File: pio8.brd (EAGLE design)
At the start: 37 x 37 mm, 35 parts, among them IC1 DS2408, X1 MSTBV3, X7 MSTBV5, X8 MSTBV5

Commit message: changing some values: 5 Ohm resistor to 5.1 Ohm (5 Ohm is not broadly available) selected different type of TVS diode with essentially the same ratings
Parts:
- D1, D10, D11, D2, D3, D4, D5, D6, D7, D8: value SMA6F7.5A -> SMAJ7.5A-LF
- R1, R10, R11, R12, R13, R14, R15, R16, R19, R2: value 5 -> 5.1
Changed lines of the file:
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@@
 <attribute name="NAME" x="20.217" y="16.5" size="0.6096" layer="25" rot="R180"/>
 </element>
-<element name="R1" library="rcl" package="R0402" value="5" x="34.25" y="3.25" smashed="yes" rot="R90">
+<element name="R1" library="rcl" package="R0402" value="5.1" x="34.25" y="3.25" smashed="yes" rot="R90">
 <attribute name="NAME" x="35.025" y="3.847" size="0.6096" layer="25" rot="R270"/>
 </element>
-<element name="R2" library="rcl" package="R0402" value="5" x="27.5" y="6.75" smashed="yes" rot="R90">
+<element name="R2" library="rcl" package="R0402" value="5.1" x="27.5" y="6.75" smashed="yes" rot="R90">
 <attribute name="NAME" x="27.725" y="4.665" size="0.6096" layer="25" rot="R90"/>
 </element>
@@
 <attribute name="NAME" x="26.751" y="29.969" size="0.6096" layer="25"/>
 </element>
-<element name="D8" library="diodes" package="DO214AC" value="SMA6F7.5A" x="30" y="3" smashed="yes" rot="R180">
+<element name="D8" library="diodes" package="DO214AC" value="SMAJ7.5A-LF" x="30" y="3" smashed="yes" rot="R180">
 <attribute name="NAME" x="28.19" y="2.766" size="0.6096" layer="25" ratio="10"/>
 </element>
-<element name="D1" library="diodes" package="DO214AC" value="SMA6F7.5A" x="15" y="26" smashed="yes">
+<element name="D1" library="diodes" package="DO214AC" value="SMAJ7.5A-LF" x="15" y="26" smashed="yes">
 <attribute name="NAME" x="15.91" y="25.746" size="0.6096" layer="25" ratio="10"/>
 </element>
-<element name="D2" library="diodes" package="DO214AC" value="SMA6F7.5A" x="15" y="29" smashed="yes">
+<element name="D2" library="diodes" package="DO214AC" value="SMAJ7.5A-LF" x="15" y="29" smashed="yes">
 <attribute name="NAME" x="15.81" y="28.696" size="0.6096" layer="25" ratio="10"/>
 </element>
-<element name="D3" library="diodes" package="DO214AC" value="SMA6F7.5A" x="15" y="32" smashed="yes">
+<element name="D3" library="diodes" package="DO214AC" value="SMAJ7.5A-LF" x="15" y="32" smashed="yes">
 <attribute name="NAME" x="15.87" y="31.756" size="0.6096" layer="25" ratio="10"/>
 </element>
-<element name="D4" library="diodes" package="DO214AC" value="SMA6F7.5A" x="15" y="35" smashed="yes">
+<element name="D4" library="diodes" package="DO214AC" value="SMAJ7.5A-LF" x="15" y="35" smashed="yes">
 <attribute name="NAME" x="15.76" y="34.806" size="0.6096" layer="25" ratio="10"/>
 </element>
-<element name="D5" library="diodes" package="DO214AC" value="SMA6F7.5A" x="22" y="35" smashed="yes" rot="R180">
+<element name="D5" library="diodes" package="DO214AC" value="SMAJ7.5A-LF" x="22" y="35" smashed="yes" rot="R180">
 <attribute name="NAME" x="20.19" y="34.672" size="0.6096" layer="25" ratio="10"/>
 </element>
-<element name="D6" library="diodes" package="DO214AC" value="SMA6F7.5A" x="22" y="32" smashed="yes" rot="R180">
+<element name="D6" library="diodes" package="DO214AC" value="SMAJ7.5A-LF" x="22" y="32" smashed="yes" rot="R180">
 <attribute name="NAME" x="20.062" y="31.616" size="0.6096" layer="25" ratio="10"/>
 </element>
-<element name="D7" library="diodes" package="DO214AC" value="SMA6F7.5A" x="22" y="29" smashed="yes" rot="R180">
+<element name="D7" library="diodes" package="DO214AC" value="SMAJ7.5A-LF" x="22" y="29" smashed="yes" rot="R180">
 <attribute name="NAME" x="20.036" y="28.728" size="0.6096" layer="25" ratio="10"/>
 </element>
-<element name="R10" library="rcl" package="R0402" value="5" x="16.567" y="10.643" smashed="yes" rot="R270">
+<element name="R10" library="rcl" package="R0402" value="5.1" x="16.567" y="10.643" smashed="yes" rot="R270">
 <attribute name="NAME" x="15.808" y="9.882" size="0.6096" layer="25" rot="R90"/>
 </element>
-<element name="R11" library="rcl" package="R0402" value="5" x="17.837" y="21.816" smashed="yes" rot="R90">
+<element name="R11" library="rcl" package="R0402" value="5.1" x="17.837" y="21.816" smashed="yes" rot="R90">
 <attribute name="NAME" x="18.122" y="23.061" size="0.6096" layer="25" rot="R90"/>
 </element>
-<element name="R12" library="rcl" package="R0402" value="5" x="19.117" y="21.804" smashed="yes" rot="R90">
+<element name="R12" library="rcl" package="R0402" value="5.1" x="19.117" y="21.804" smashed="yes" rot="R90">
 <attribute name="NAME" x="19.462" y="23.139" size="0.6096" layer="25" rot="R90"/>
 </element>
-<element name="R13" library="rcl" package="R0402" value="5" x="20.377" y="21.816" smashed="yes" rot="R90">
+<element name="R13" library="rcl" package="R0402" value="5.1" x="20.377" y="21.816" smashed="yes" rot="R90">
 <attribute name="NAME" x="20.108" y="24.729" size="0.6096" layer="25" rot="R270"/>
 </element>
-<element name="R14" library="rcl" package="R0402" value="5" x="21.637" y="21.834" smashed="yes" rot="R90">
+<element name="R14" library="rcl" package="R0402" value="5.1" x="21.637" y="21.834" smashed="yes" rot="R90">
 <attribute name="NAME" x="21.792" y="23.239" size="0.6096" layer="25" rot="R90"/>
 </element>
-<element name="R15" library="rcl" package="R0402" value="5" x="24.157" y="21.774" smashed="yes" rot="R90">
+<element name="R15" library="rcl" package="R0402" value="5.1" x="24.157" y="21.774" smashed="yes" rot="R90">
 <attribute name="NAME" x="24.562" y="22.929" size="0.6096" layer="25" rot="R90"/>
 </element>
-<element name="R16" library="rcl" package="R0402" value="5" x="27.5" y="18.25" smashed="yes" rot="R90">
+<element name="R16" library="rcl" package="R0402" value="5.1" x="27.5" y="18.25" smashed="yes" rot="R90">
 <attribute name="NAME" x="27.865" y="15.615" size="0.6096" layer="25" rot="R90"/>
 </element>
@@
 <attribute name="NAME" x="26.615" y="27.012" size="0.6096" layer="25"/>
 </element>
-<element name="D10" library="diodes" package="DO214AC" value="SMA6F7.5A" x="22" y="26" smashed="yes" rot="R180">
+<element name="D10" library="diodes" package="DO214AC" value="SMAJ7.5A-LF" x="22" y="26" smashed="yes" rot="R180">
 <attribute name="NAME" x="20" y="25.5" size="0.6096" layer="25" ratio="10"/>
 </element>
-<element name="D11" library="diodes" package="DO214AC" value="SMA6F7.5A" x="27.01" y="11.96" smashed="yes" rot="R270">
+<element name="D11" library="diodes" package="DO214AC" value="SMAJ7.5A-LF" x="27.01" y="11.96" smashed="yes" rot="R270">
 <attribute name="NAME" x="27.454" y="9.9" size="0.6096" layer="25" ratio="10" rot="R90"/>
 </element>
-<element name="R19" library="rcl" package="R0402" value="5" x="26" y="18.25" smashed="yes" rot="R90">
+<element name="R19" library="rcl" package="R0402" value="5.1" x="26" y="18.25" smashed="yes" rot="R90">
 <attribute name="NAME" x="26.365" y="15.615" size="0.6096" layer="25" rot="R90"/>
 <attribute name="VALUE" x="27.905" y="17.615" size="1.27" layer="27" rot="R90"/>

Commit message: rotating connectors to resolve issue #1 while maintaining IO and GND/VCC pinout but rotating pinout for the one wire connector (to keep the pin numbering the same as other 1-wire devices have)
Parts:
- moved X1 0.70 mm to (18.5, 4.70), turned to 180 degrees
- moved X8 0.63 mm to (32.3, 18.5), turned to 270 degrees
- moved X7 0.60 mm to (4.70, 18.5), turned to 90 degrees
- moved D9 0.25 mm to (22.9, 10.4)
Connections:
- net GND: now also X8.5; no longer X8.1
- net N$1: now also X7.1; no longer X7.5
- net N$11: now also X8.4; no longer X8.2
- net N$2: now also X7.2; no longer X7.4
- net N$4: now also X7.4; no longer X7.2
- net N$5: now also X7.5; no longer X7.1
- net N$6: now also X8.1; no longer X8.5
- net N$7: now also X8.2; no longer X8.4
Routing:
- net N$9: track 8.07 -> 23.4 mm
- net N$10: track 18.8 -> 20.9 mm
- net N$20: track 24.3 -> 25.7 mm
- net GND: track 71.8 -> 70.5 mm
- net N$12: track 25.1 -> 25.8 mm
- net N$7: track 26.8 -> 26.2 mm
- net N$6: track 26.5 -> 25.9 mm
- net N$11: track 79.8 -> 79.2 mm
- net N$5: track 47.7 -> 47.1 mm
- net N$4: track 37.2 -> 36.6 mm
- net N$3: track 35.6 -> 35.0 mm
- net N$2: track 34.4 -> 33.8 mm
- net N$1: track 46.3 -> 45.7 mm

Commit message: changing the connector solution for the digital i/o's - now using spring clamp terminals instead of pluggable screw terminals. The new ones should reduce the width. Also turning back the 3 pin connector so that the screw terminal pints inward
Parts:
- removed X7, X8: MSTBV5, con-phoenix-508:MSTBV5
- added X2, X3: SPRING_CLAMP_5_AST215, connectors:AST215_5
- turned X1 to 0 degrees
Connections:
- net GND: now also X2.5A, X2.5B; no longer X8.5
- net N$1: now also X3.1A, X3.1B; no longer X7.1
- net N$11: now also X2.4A, X2.4B; no longer X8.4
- net N$12: now also X2.3A, X2.3B; no longer X8.3
- net N$2: now also X3.2A, X3.2B; no longer X7.2
- net N$3: now also X3.3A, X3.3B; no longer X7.3
- net N$4: now also X3.4A, X3.4B; no longer X7.4
- net N$5: now also X3.5A, X3.5B; no longer X7.5
- net N$6: now also X2.1A, X2.1B; no longer X8.1
- net N$7: now also X2.2A, X2.2B; no longer X8.2
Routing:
- net N$9: track 23.4 -> 8.36 mm
- net N$3: track 35.0 -> 44.7 mm
- net N$4: track 36.6 -> 46.1 mm
- net N$5: track 47.1 -> 56.0 mm
- net GND: track 70.5 -> 62.9 mm
- net N$7: track 26.2 -> 30.3 mm
- net N$12: track 25.8 -> 29.8 mm
- net N$6: track 25.9 -> 28.9 mm
- net N$2: track 33.8 -> 36.8 mm
- net N$11: track 79.2 -> 82.1 mm
- net N$1: track 45.7 -> 48.6 mm

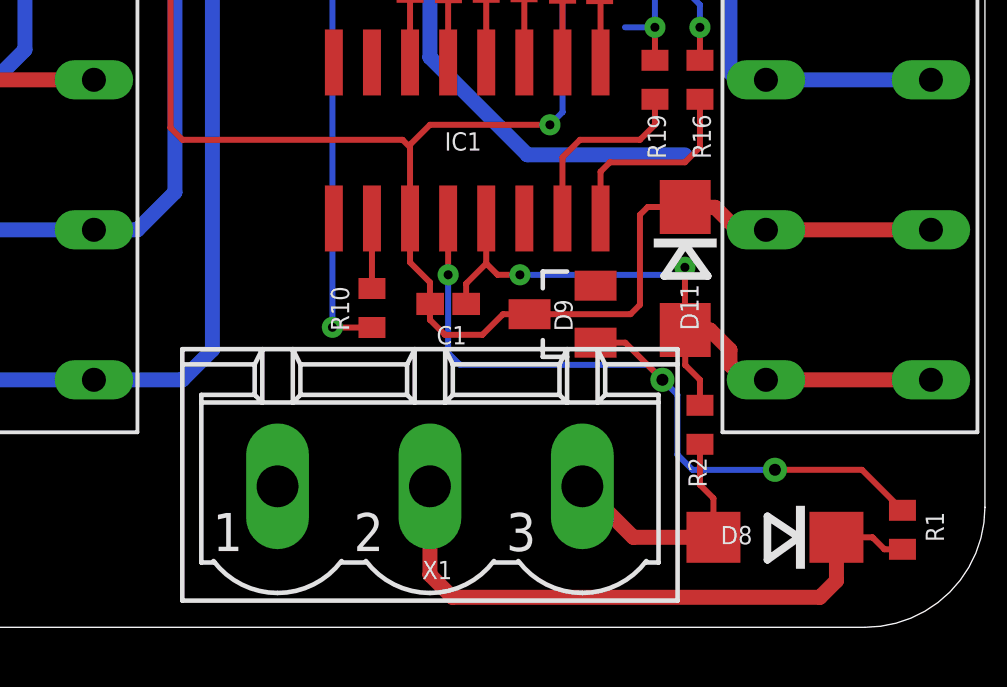
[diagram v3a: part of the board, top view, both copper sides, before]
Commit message: changing 1-wire connector to a spring clamp type
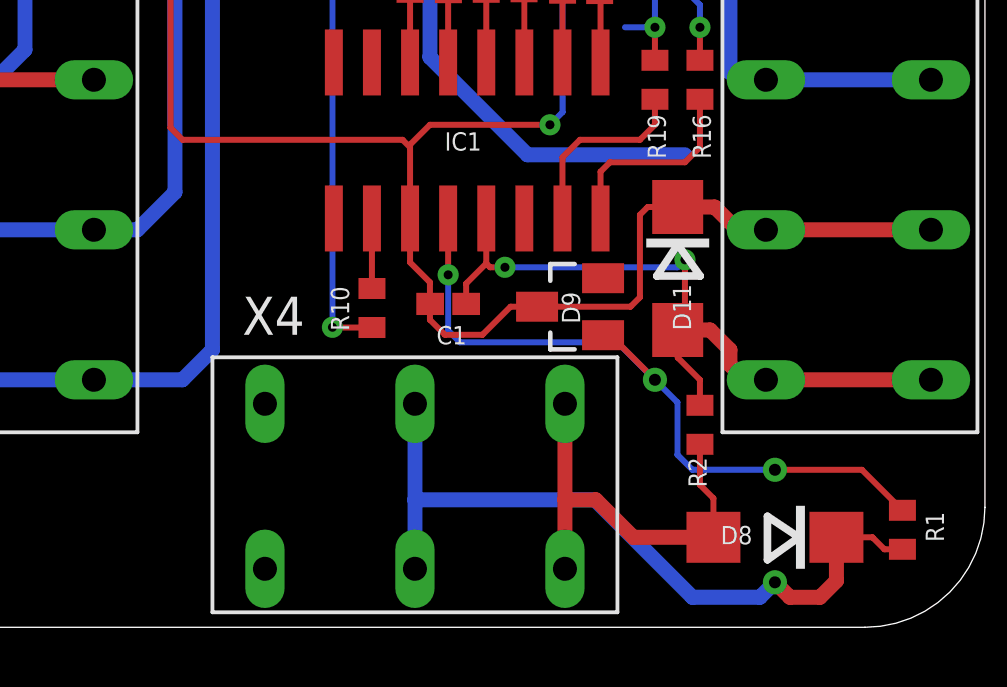
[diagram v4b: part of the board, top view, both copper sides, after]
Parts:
- removed X1: MSTBV3, con-phoenix-508:MSTBV3
- added X4: SPRING_CLAMP_3_AST215, connectors:AST215_3
- moved D9 0.35 mm to (23.2, 10.7)
- moved D11 0.25 mm to (26.8, 12.0)
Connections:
- net N$10: now also X4.2A, X4.2B; no longer X1.2
- net N$9: now also X4.3A, X4.3B; no longer X1.3
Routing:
- net N$9: track 8.36 -> 14.3 mm
- net N$10: track 20.9 -> 25.4 mm, vias 0 -> 1
- net N$20: track 25.7 -> 24.7 mm
- net GND: track 62.9 -> 63.5 mm
